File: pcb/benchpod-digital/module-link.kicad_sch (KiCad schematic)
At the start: 15 parts, among them CN1 KH-FPC1.0-H2.0SMT-24P-QCHF, U59 TPS259470ARPWR

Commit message: digital v3r3: always-on USB-A (USB2) to power the optional Wi-Fi bridge
USB1 stays the target-power USB-A (it follows eFuse 1 and power-cycles with
the DUT). USB2 is a second USB-A, same part, for the back panel next to the
RJ45: always-on 5 V for the Wi-Fi bridge (power only, data goes over RJ45),
as decided in benchpod-private enclosure/wifi-bridge.md (USB-A rather than a
second USB-C, so nobody plugs the laptop into the wrong port).

- eFuse U60, a copy of U26/U59 (TPS259470A): about 1 A limit, soft start,
  OVLO; EN pulled up, so it is on at power-up and older firmware keeps it on.
- STM32 PD14 BRIDGE_PWR_EN (low = off, to power-cycle a hung bridge),
  PD15 BRIDGE_PWR_FLT#, PG2 BRIDGE_PWR_PG. D+/D- tied, like USB1.
- On the Module link sheet (renamed "Module link, bridge power"); no new BOM
  lines.

Co-Authored-By: Claude Opus 5.5 <noreply@anthropic.com>
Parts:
- added C267: 10n, Capacitor_SMD:C_0402_1005Metric, symbol Device:C
- added C268: 3.3n, Capacitor_SMD:C_0402_1005Metric, symbol Device:C
- added C269: 10u, Capacitor_SMD:C_0603_1608Metric, symbol Device:C
- added C270, C272: 100n, Capacitor_SMD:C_0402_1005Metric, symbol Device:C
- added C271: 1u, Capacitor_SMD:C_0402_1005Metric, symbol Device:C
- added R187: 1.65k, Resistor_SMD:R_0402_1005Metric, symbol Device:R
- added R188: 37.4k, Resistor_SMD:R_0402_1005Metric, symbol Device:R
- added R189, R190, R191, R192: 10k, Resistor_SMD:R_0402_1005Metric, symbol Device:R
- added U60: TPS259470ARPWR, lcsc:VQFN-10_L2.0-W2.0-P0.45-TL, symbol lcsc_lib:TPS259470ARPWR
- added USB2: AF 90° WJDG, lcsc_footprints:C456018_USB-A-TH_AF-WJDG, symbol lcsc_plugin:AF_90°_WJDG
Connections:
- net +3V3: now also R190.1, R191.1, R192.1
- net +5V: now also C271.1, C272.1, R188.1, U60.5 (IN)
- net GND: now also C267.2, C268.2, C269.2, C270.2, C271.2, C272.2, R187.2, R189.2, U60.8 (GND), USB2.4 (GND), USB2.5 (SHLD)
- new net +5V_BRIDGE: C269.1, C270.1, U60.6 (OUT), USB2.1 (VCC)
- new net BRIDGE_PWR_EN: R190.2, U60.1 (EN/UVLO)
- new net BRIDGE_PWR_FLT#: R191.2, U60.4 (~{FLT}/PGTH)
- new net BRIDGE_PWR_PG: R192.2, U60.3 (PG/AUXOFF)
- new net BR_DVDT: C267.1, U60.7 (DVDT)
- new net BR_ILM: R187.1, U60.9 (ILM)
- new net BR_ITIMER: C268.1, U60.10 (ITIMER)
- new net BR_OVLO: R188.2, R189.1, U60.2 (OVLO/OVCSEL)
- new net BR_USB_DPDM: USB2.2 (D-), USB2.3 (D+)

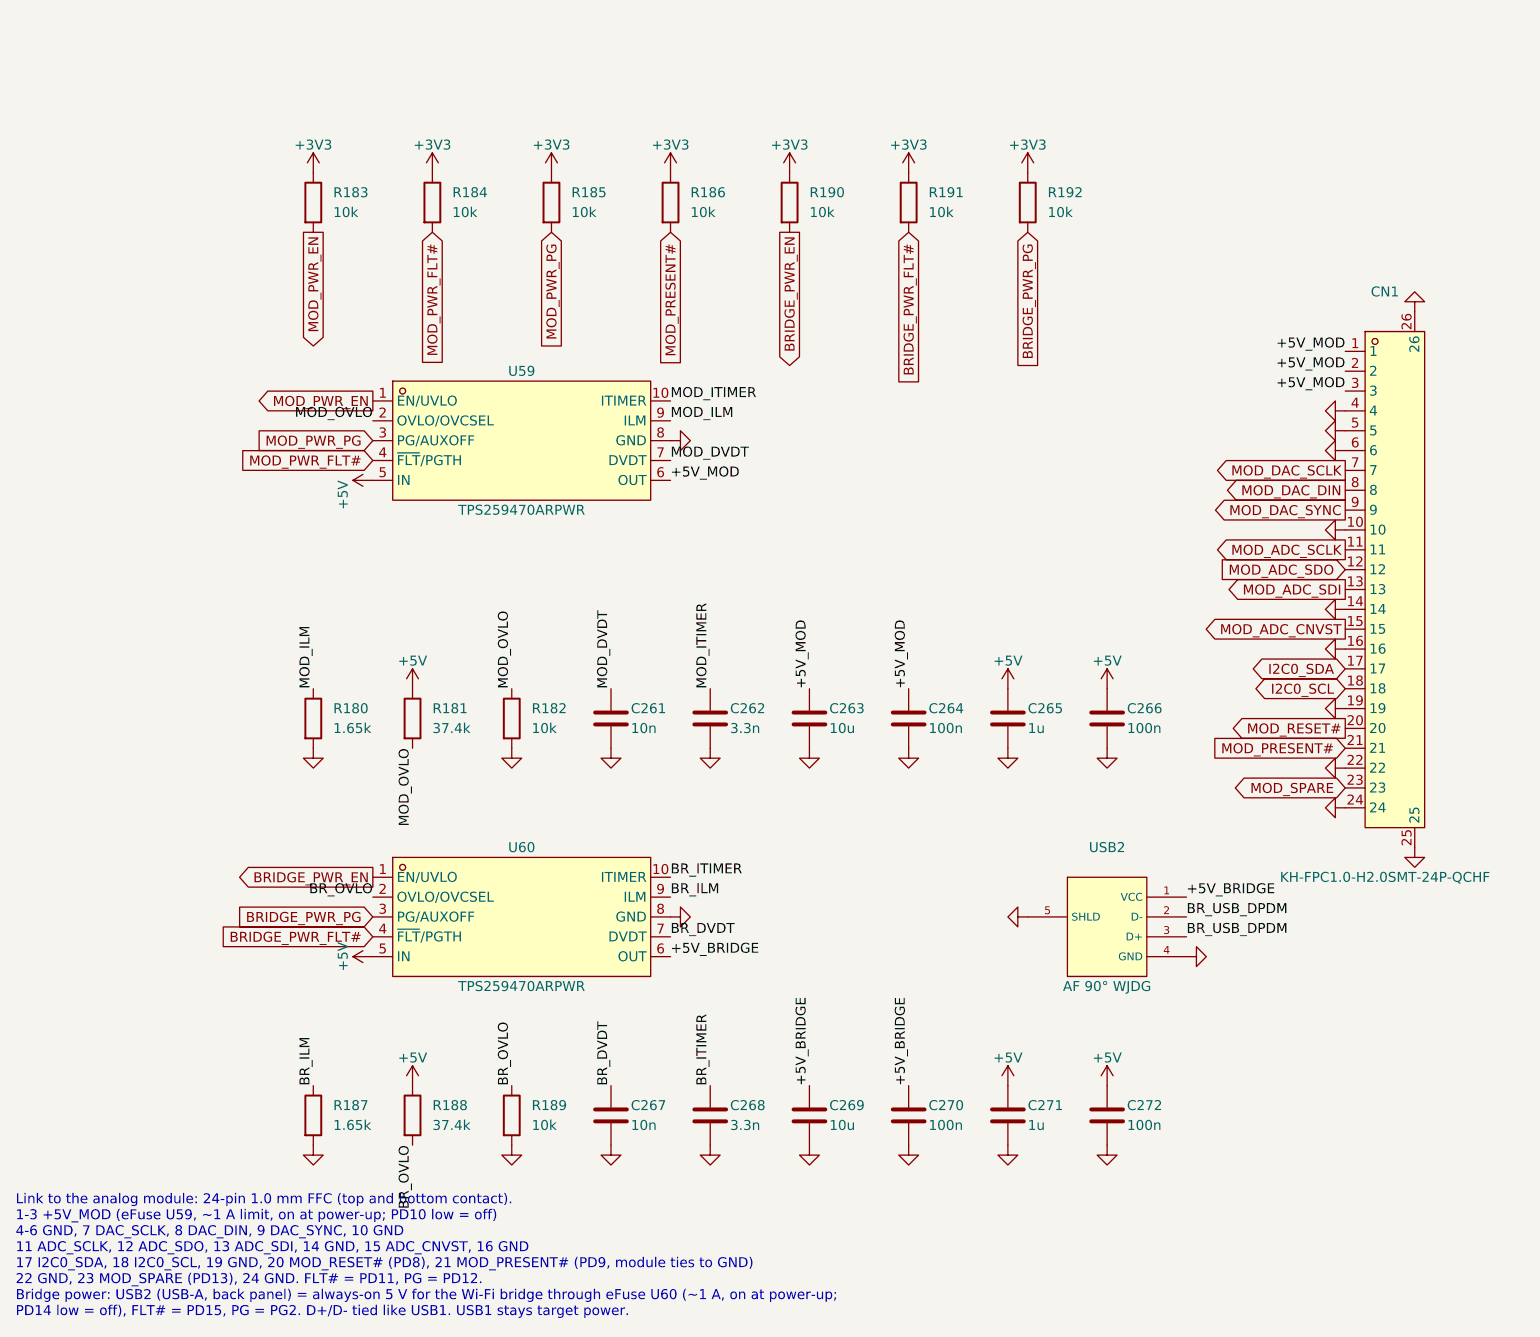
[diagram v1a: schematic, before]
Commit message: digital v3r3: own I2C bus for the module; module sheet uses hierarchical labels
- CN1 pins 17/18 move from the pod's internal I2C0 bus to a separate bus for
  the analog module: MOD_I2C_SDA = PF0, MOD_I2C_SCL = PF1 (STM32 I2C2, AF4),
  4.7k pull-ups R193/R194 to +3V3 (existing 4.7k line). A fault on the module
  or its cable can no longer hang the INA226 and TCA9554 bus.
- The "Module link, bridge power" sheet now connects through hierarchical
  labels and sheet pins instead of global labels: the sheet box on the root
  sheet moved to the free space at the top (152.4, 25.4), 50.8 x 25.4, with
  the 9 FPGA/I2C lines on the left and the 9 STM32 control lines on the right.
- Removes the old I2C0 stubs at the former CN1 position, which also clears the
  same-local-and-global-label ERC warning.

Netlist: only CN1 17/18, U5 PF0/PF1 and the two pull-ups change; every other
net keeps its connections.

Co-Authored-By: Claude Opus 5.5 <noreply@anthropic.com>
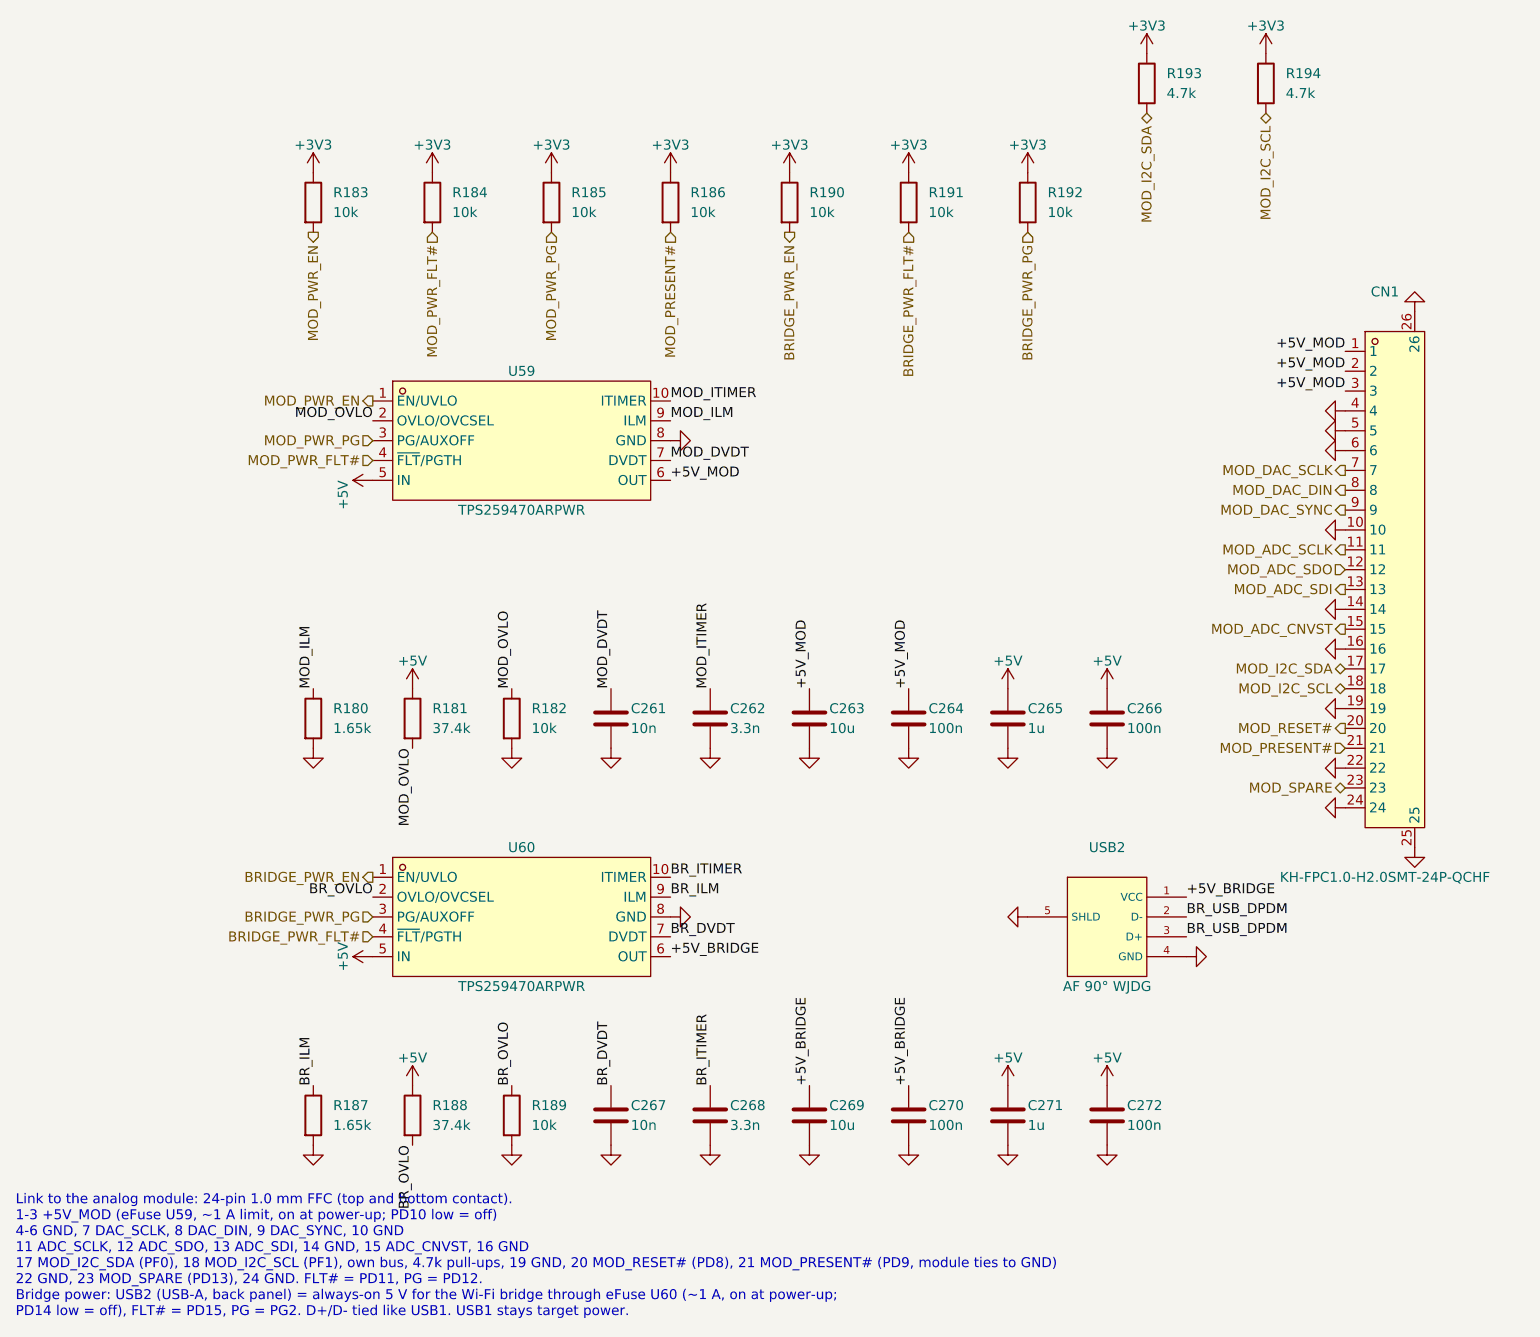
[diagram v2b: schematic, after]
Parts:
- added R193, R194: 4.7k, Resistor_SMD:R_0402_1005Metric, symbol Device:R
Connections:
- net +3V3: now also R193.1, R194.1
- net I2C0_SCL renamed MOD_I2C_SCL
- net MOD_I2C_SCL: now also R194.2
- net I2C0_SDA renamed MOD_I2C_SDA
- net MOD_I2C_SDA: now also R193.2
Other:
- note added: "Link to the analog module: 24-pin 1.0 mm FFC (top and bottom contact). 1-3 +5V_MOD (eFuse U59, ~1 A limit, on at power-up; PD10 low = off) 4-6 GND, 7 DAC_SCLK, 8 DAC_DIN, 9 DAC_SYNC, 10 GND 11 ADC_SCLK, 12 ADC_SDO, 13 ADC_SDI, 14 GND, 15 ADC_CNVST, 16 GND 17 MOD_I2C_SDA (PF0), 18 MOD_I2C_SCL (PF1), own bus, 4.7k pull-ups, 19 GND, 20 MOD_RESET# (PD8), 21 MOD_PRESENT# (PD9, module ties to GND) 22 G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"
- note removed: "Link to the analog module: 24-pin 1.0 mm FFC (top and bottom contact). 1-3 +5V_MOD (eFuse U59, ~1 A limit, on at power-up; PD10 low = off) 4-6 GND, 7 DAC_SCLK, 8 DAC_DIN, 9 DAC_SYNC, 10 GND 11 ADC_SCLK, 12 ADC_SDO, 13 ADC_SDI, 14 GND, 15 ADC_CNVST, 16 GND 17 I2C0_SDA, 18 I2C0_SCL, 19 GND, 20 MOD_RESET# (PD8), 21 MOD_PRESENT# (PD9, module ties to GND) 22 GND, 23 MOD_SPARE (PD13), 24 GND. FLT# = PD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"
